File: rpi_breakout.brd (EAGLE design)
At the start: 34.3 x 49.5 mm, 20 parts

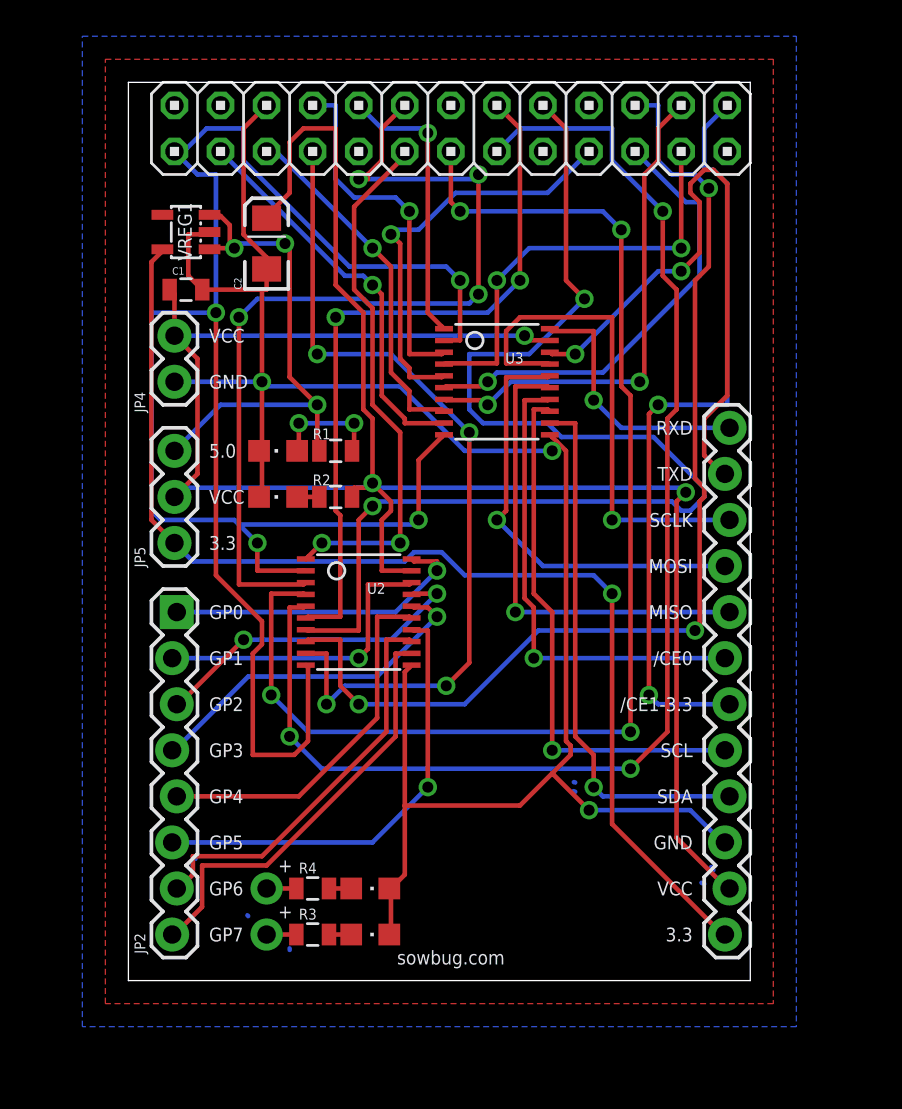
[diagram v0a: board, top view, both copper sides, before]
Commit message: New README. Some labeling tweaks on the board.
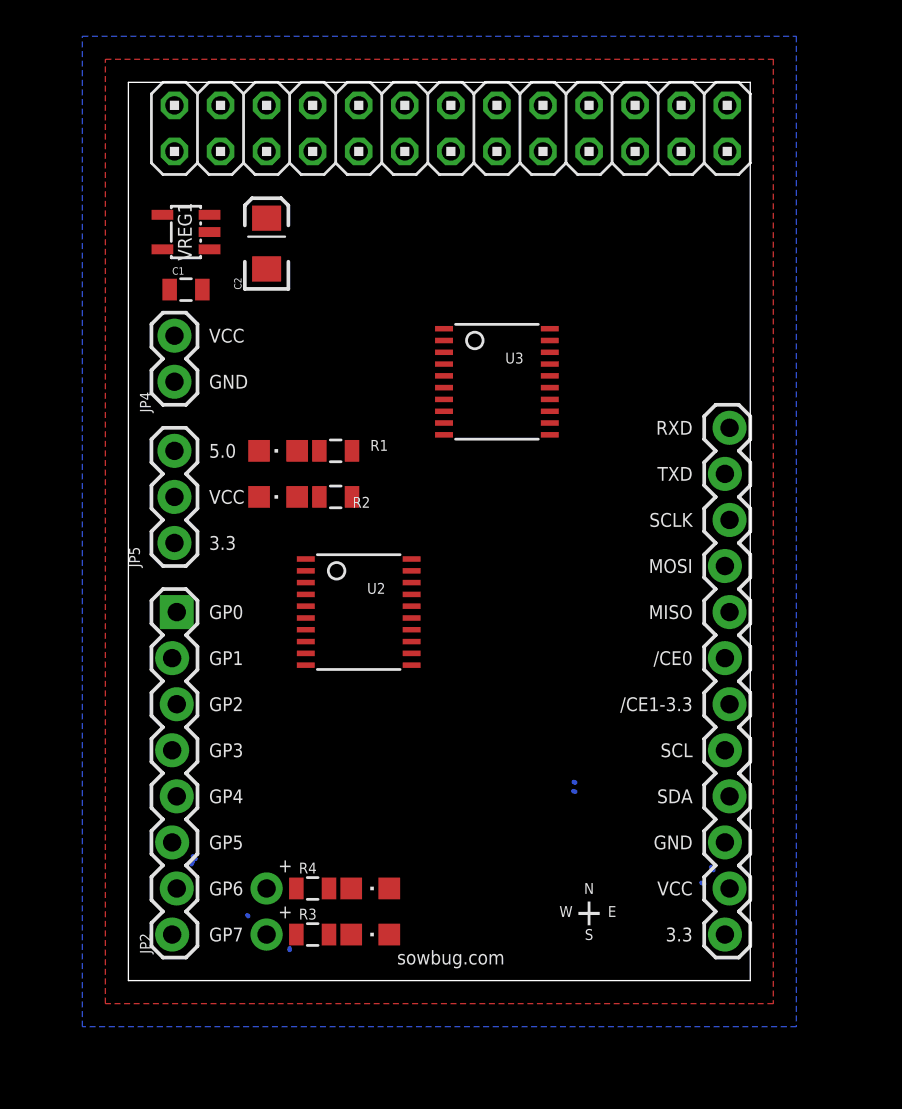
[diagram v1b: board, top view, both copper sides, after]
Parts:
- LED1: value CONN -> CONNECTED
- LED2: value POWER -> IO-POWER
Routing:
- net VCC: track 122.5 -> 0.00 mm, vias 3 -> 0
- net GND: track 109.2 -> 0.00 mm, vias 3 -> 0
- net 3V3_RPI: track 109.0 -> 0.00 mm, vias 4 -> 0
- net GPIO_3: track 72.3 -> 0.00 mm, vias 3 -> 0
- net GPIO_2: track 68.9 -> 0.00 mm, vias 4 -> 0
- net GPIO_5: track 66.5 -> 0.00 mm, vias 2 -> 0
- net 3.3V: track 64.1 -> 0.00 mm, vias 1 -> 0
- net GPIO_6: track 59.0 -> 0.00 mm, vias 3 -> 0
- net GPIO_1: track 51.1 -> 0.00 mm, vias 4 -> 0
- net GPIO_7: track 46.9 -> 0.00 mm, vias 4 -> 0
- net /SPI_CE1: track 42.5 -> 0.00 mm, vias 2 -> 0
- net GPIO_4: track 39.7 -> 0.00 mm, vias 2 -> 0
- net TXDV: track 34.4 -> 0.00 mm, vias 2 -> 0
- net SCLV0: track 29.7 -> 0.00 mm, vias 1 -> 0
- net SDAV0: track 29.6 -> 0.00 mm, vias 1 -> 0
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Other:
- board text added: "E"
- board text added: "N"
- board text added: "S"
- board text added: "W"

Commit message: Rough route with 5 vias, some headers pulled inward
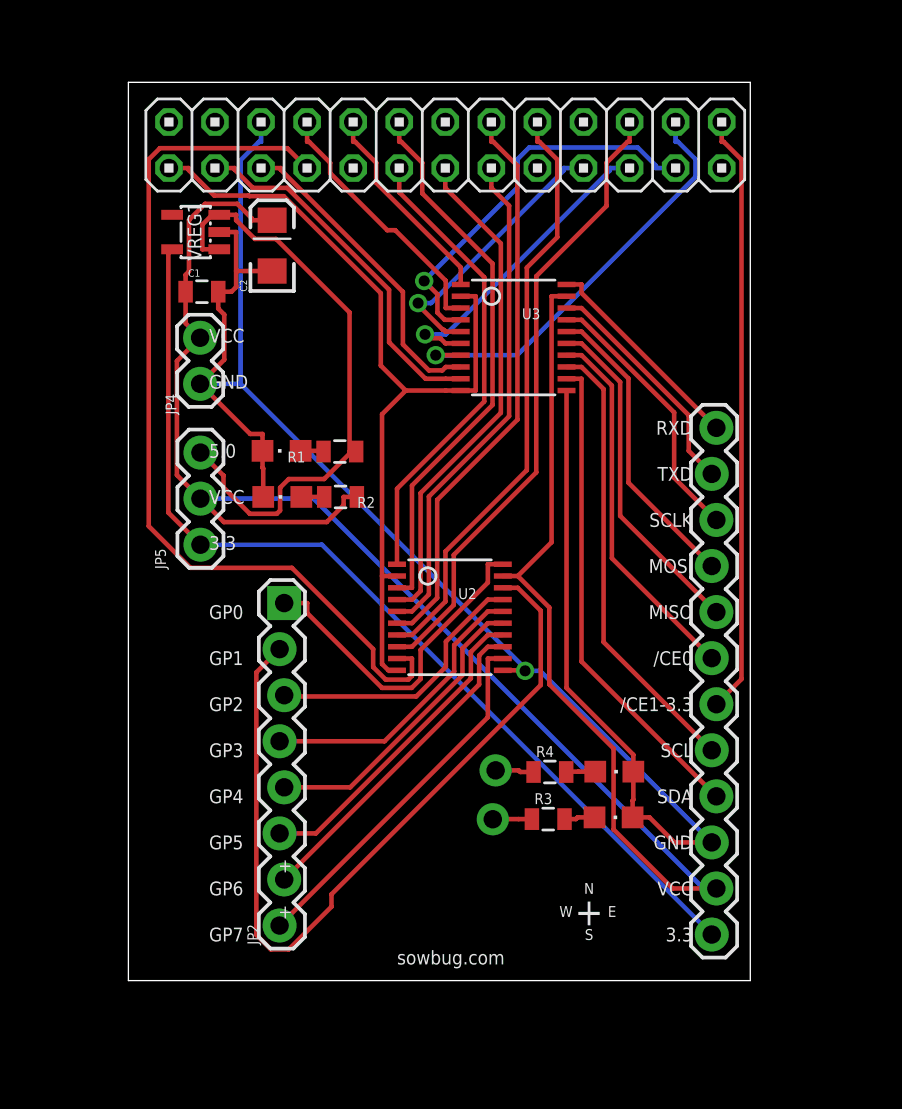
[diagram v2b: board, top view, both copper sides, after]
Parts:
- moved LED4 14.9 mm to (26.8, 11.5)
- moved LED3 14.9 mm to (26.8, 9.00)
- moved R4 14.6 mm to (23.2, 11.5)
- moved R3 14.5 mm to (23.1, 8.91)
- moved JP7 14.2 mm to (20.2, 11.6)
- moved JP6 14.0 mm to (20.1, 8.90)
- moved JP2 5.94 mm to (8.46, 20.8)
- moved U2 5.04 mm to (17.7, 20.0)
- moved U3 2.61 mm to (21.2, 35.5)
- moved JP5 1.44 mm to (3.97, 24.0)
- moved JP4 1.42 mm to (3.95, 35.4)
- moved JP1 0.97 mm to (17.5, 46.1)
- moved C1 0.89 mm to (4.05, 38.0)
- moved JP3 0.73 mm to (32.3, 2.54)
- moved VREG1 0.54 mm to (3.71, 41.3)
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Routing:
- net VCC: track 0.00 -> 110.6 mm
- net GND: track 0.00 -> 105.9 mm, vias 0 -> 1
- net 3.3V: track 0.00 -> 54.2 mm
- net GPIO_7: track 0.00 -> 50.1 mm
- net 3V3_RPI: track 0.00 -> 47.8 mm
- net GPIOV_1: track 0.00 -> 45.5 mm
- net GPIO_6: track 0.00 -> 34.8 mm
- net 5V: track 0.00 -> 33.3 mm
- net /SPI_CE1: track 0.00 -> 33.2 mm
- net GPIO_5: track 0.00 -> 32.9 mm
- net GPIO_4: track 0.00 -> 31.5 mm
- net GPIO_1: track 0.00 -> 30.5 mm
- net GPIO_2: track 0.00 -> 27.9 mm
- net GPIO_3: track 0.00 -> 27.9 mm
- net SDAV0: track 0.00 -> 26.9 mm
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- removed copper zone on layer 1, net N$7
- removed copper zone on layer 16, net N$8

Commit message: Rotated GPIO pins, slightly tighter routing, 4 vias
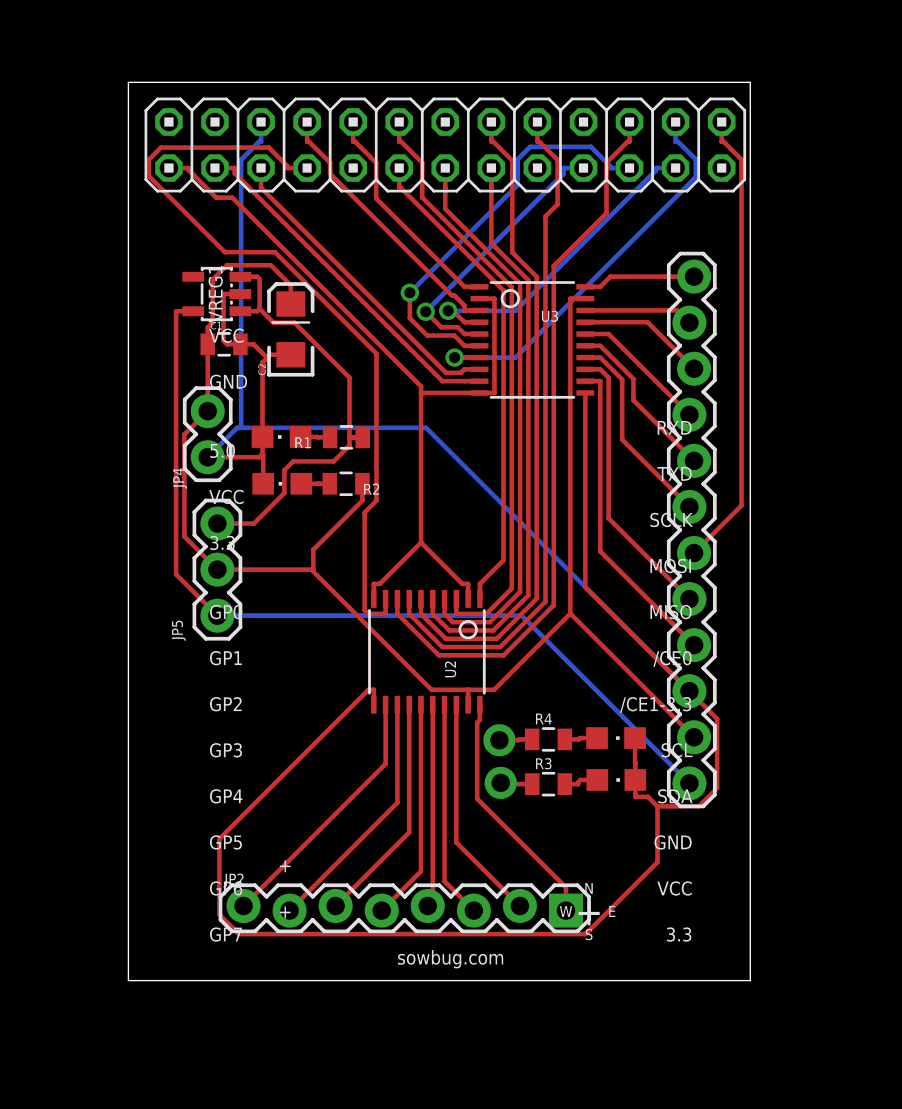
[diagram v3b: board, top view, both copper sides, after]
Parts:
- moved JP2 23.0 mm to (24.1, 3.99), turned to 180 degrees
- moved JP3 8.43 mm to (31.1, 10.9)
- moved C2 4.73 mm to (8.96, 35.9)
- moved JP4 4.07 mm to (4.37, 31.4)
- moved JP5 4.02 mm to (4.91, 20.1)
- moved VREG1 3.61 mm to (4.87, 37.9)
- moved C1 3.15 mm to (5.28, 35.1)
- moved U2 2.29 mm to (16.5, 18.1), turned to 180 degrees
- moved LED3 2.07 mm to (26.9, 11.1)
- moved JP6 2.05 mm to (20.5, 10.9)
- moved R3 1.93 mm to (23.2, 10.8)
- moved LED4 1.85 mm to (26.9, 13.4)
- moved R4 1.80 mm to (23.2, 13.3)
- moved JP7 1.67 mm to (20.5, 13.3)
- moved U3 1.05 mm to (22.3, 35.3)
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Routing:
- net GND: track 105.9 -> 147.9 mm, vias 1 -> 0
- net GPIOV_1: track 45.5 -> 12.5 mm
- net VCC: track 110.6 -> 82.0 mm
- net SDAV0: track 26.9 -> 17.5 mm
- net SPI_MISOV: track 18.7 -> 9.31 mm
- net SCLV0: track 24.9 -> 15.5 mm
- net /SPI_CEV0: track 20.5 -> 11.1 mm
- net SPI_MOSIV: track 16.7 -> 7.59 mm
- net 5V: track 33.3 -> 25.4 mm
- net SPI_SCLKV: track 14.9 -> 7.06 mm
- net /SPI_CE1: track 33.2 -> 25.4 mm
- net TXDV: track 12.9 -> 6.02 mm
- net GPIO_7: track 50.1 -> 43.5 mm
- net GPIOV_7: track 20.3 -> 14.3 mm
- net 3.3V: track 54.2 -> 48.5 mm
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
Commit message: Smaller still.  Power section moved S.  Board size limited by two long headers.  3 vias.
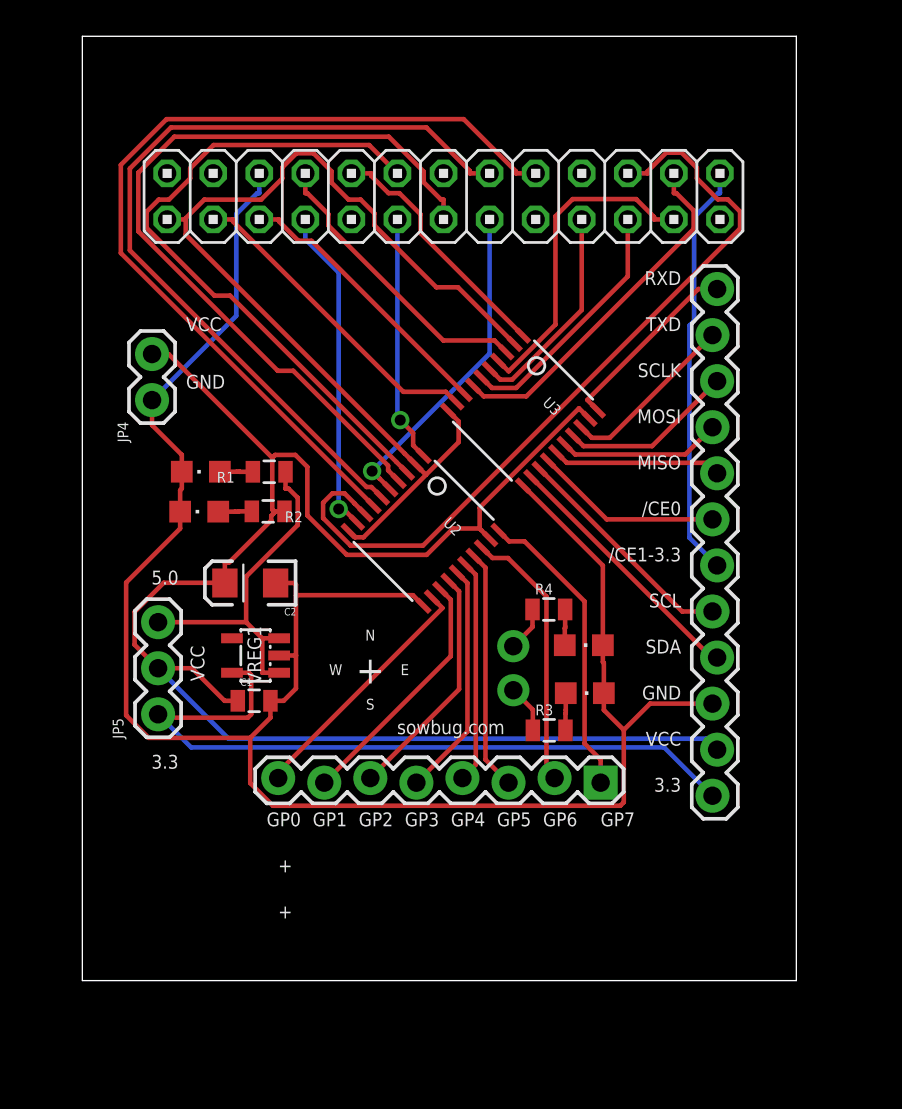
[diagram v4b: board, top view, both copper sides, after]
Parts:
- moved VREG1 20.0 mm to (7.01, 17.9)
- moved C1 19.7 mm to (6.93, 15.4)
- moved C2 14.2 mm to (6.72, 21.9), turned to 180 degrees
- moved JP2 7.31 mm to (26.0, 11.0)
- moved R4 7.17 mm to (23.2, 20.5)
- moved U2 6.67 mm to (16.3, 24.8), turned to 225 degrees
- moved JP5 6.35 mm to (1.64, 14.7)
- moved LED4 5.42 mm to (25.1, 18.5)
- moved JP7 5.24 mm to (21.2, 18.4)
- moved JP6 5.16 mm to (21.2, 16.0)
- moved LED3 5.09 mm to (25.2, 15.8)
- moved LED1 4.85 mm to (4.00, 28.1)
- moved LED2 4.83 mm to (3.90, 25.9)
- moved R1 4.66 mm to (7.76, 28.1)
- moved R2 4.56 mm to (7.71, 25.9)
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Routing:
- net GND: track 147.9 -> 109.9 mm
- net GPIO_7: track 43.5 -> 18.1 mm, vias 0 -> 1
- net GPIO_3: track 31.7 -> 18.0 mm, vias 0 -> 1
- net GPIO_0: track 26.7 -> 13.6 mm, vias 0 -> 1
- net GPIO_2: track 31.0 -> 44.0 mm
- net GPIO_5: track 37.4 -> 49.8 mm
- net GPIO_4: track 36.1 -> 46.0 mm
- net 3V3_RPI: track 46.4 -> 56.1 mm
- net VCC: track 82.0 -> 91.4 mm
- net SPI_MISO: track 22.7 -> 14.0 mm, vias 1 -> 0
- net 3.3V: track 48.5 -> 41.0 mm
- net 5V: track 25.4 -> 19.7 mm
- net GPIO_1: track 32.8 -> 37.2 mm
- net RXDV: track 6.23 -> 10.5 mm
- net GPIO_6: track 40.0 -> 44.1 mm
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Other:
- board size 34.3 x 49.5 mm -> 39.4 x 52.1 mm

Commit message: v0.0.2, restored polygons, fixed up silkscreen
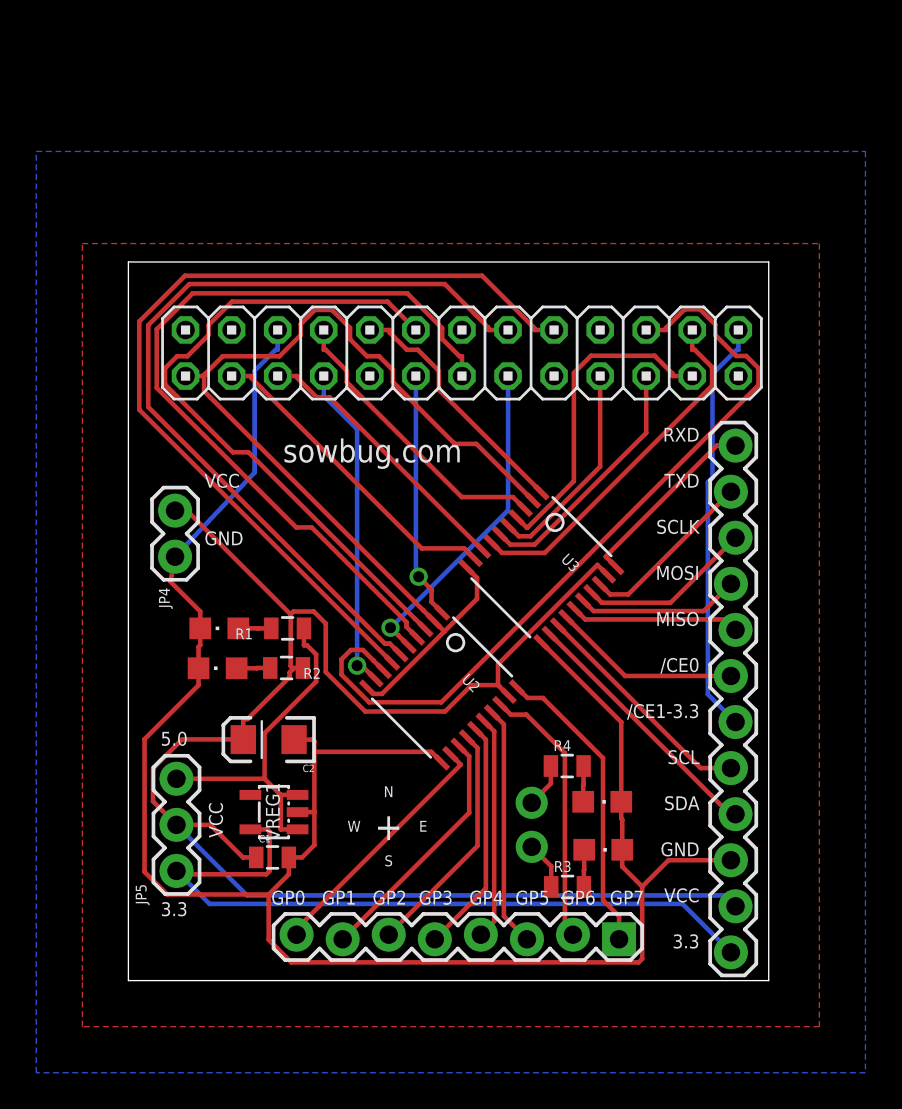
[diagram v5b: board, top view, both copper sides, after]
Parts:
- moved JP4 8.73 mm to (2.57, 25.9)
- moved LED2 8.70 mm to (4.92, 17.2)
- moved U3 8.70 mm to (22.8, 22.8)
- moved C1 8.70 mm to (7.95, 6.79)
- moved JP3 8.70 mm to (33.4, 1.56)
- moved C2 8.70 mm to (7.74, 13.3)
- moved JP2 8.70 mm to (27.1, 2.41)
- moved JP5 8.70 mm to (2.65, 6.05)
- moved JP6 8.70 mm to (22.2, 7.37)
- moved JP7 8.70 mm to (22.2, 9.80)
- moved LED1 8.70 mm to (5.01, 19.4)
- moved LED3 8.70 mm to (26.2, 7.21)
- moved LED4 8.70 mm to (26.1, 9.86)
- moved R1 8.70 mm to (8.78, 19.4)
- moved R2 8.70 mm to (8.72, 17.2)
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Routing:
- added copper zone on layer 1, net GND
- added copper zone on layer 16, net VCC
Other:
- board size 39.4 x 52.1 mm -> 35.3 x 39.6 mm
- board text added: "Raspberry Pi Breakout Board v0.0.2"
- board text removed: "Raspberry Pi Breakout Board v0.0.1"

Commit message: power/gnd and skinny net classes.  mitered corners.  better polygon isolation.  2 vias
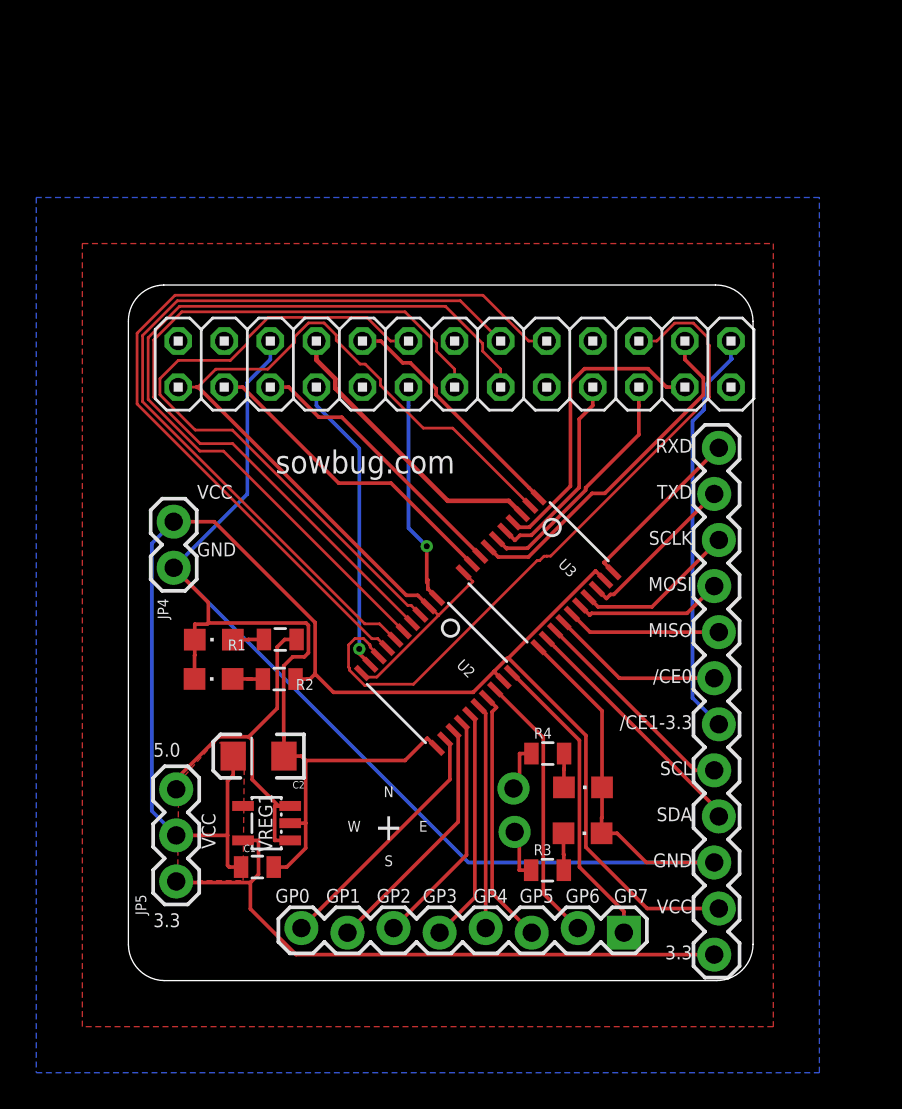
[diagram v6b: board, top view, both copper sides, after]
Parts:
- moved LED3 1.46 mm to (25.0, 8.12)
- moved R3 1.45 mm to (23.1, 6.09)
- moved LED4 1.33 mm to (25.1, 10.7)
- moved JP7 1.28 mm to (21.2, 10.6)
- moved R4 1.28 mm to (23.1, 12.5)
- moved JP6 1.25 mm to (21.3, 8.20)
- moved C2 1.07 mm to (7.18, 12.4)
- moved C1 0.99 mm to (7.11, 6.26)
- moved JP3 0.93 mm to (32.4, 1.43)
- moved U2 0.85 mm to (17.0, 17.0)
- moved R1 0.73 mm to (8.37, 18.8)
- moved R2 0.73 mm to (8.32, 16.6)
- moved VREG1 0.73 mm to (7.62, 8.68)
- moved JP1 0.73 mm to (18.0, 34.0)
- moved LED1 0.69 mm to (4.71, 18.8)
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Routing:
- net GPIO_3: track 18.0 -> 45.6 mm, vias 1 -> 0
- net VCC: track 91.1 -> 83.3 mm
- net GPIO_6: track 44.1 -> 38.4 mm
- net 3.3V: track 41.0 -> 35.6 mm
- net 3V3_RPI: track 56.1 -> 53.2 mm
- net GPIO_5: track 49.8 -> 47.8 mm
- net GPIO_2: track 44.0 -> 42.3 mm
- net GPIO_7: track 18.1 -> 16.5 mm
- net GPIO_4: track 46.0 -> 44.5 mm
- net GND: track 109.8 -> 108.4 mm
- net GPIO_0: track 13.6 -> 12.5 mm
- net GPIO_1: track 37.2 -> 36.1 mm
- net SPI_SCLK: track 17.9 -> 16.9 mm
- net GPIOV_2: track 13.3 -> 14.2 mm
- net SPI_MISOV: track 9.35 -> 8.52 mm
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- added copper zone on layer 1, net VCC
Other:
- board size 35.3 x 39.6 mm -> 34.4 x 38.4 mm
